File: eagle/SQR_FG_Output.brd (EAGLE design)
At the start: 96.2 x 58.4 mm, 35 parts, among them IC1 MEGA328P, IC2 NJM7032, IC3 7805T, IC4 TLV1117-33, Q1 16MHz, T1 2SK4017, T2 2SK4017

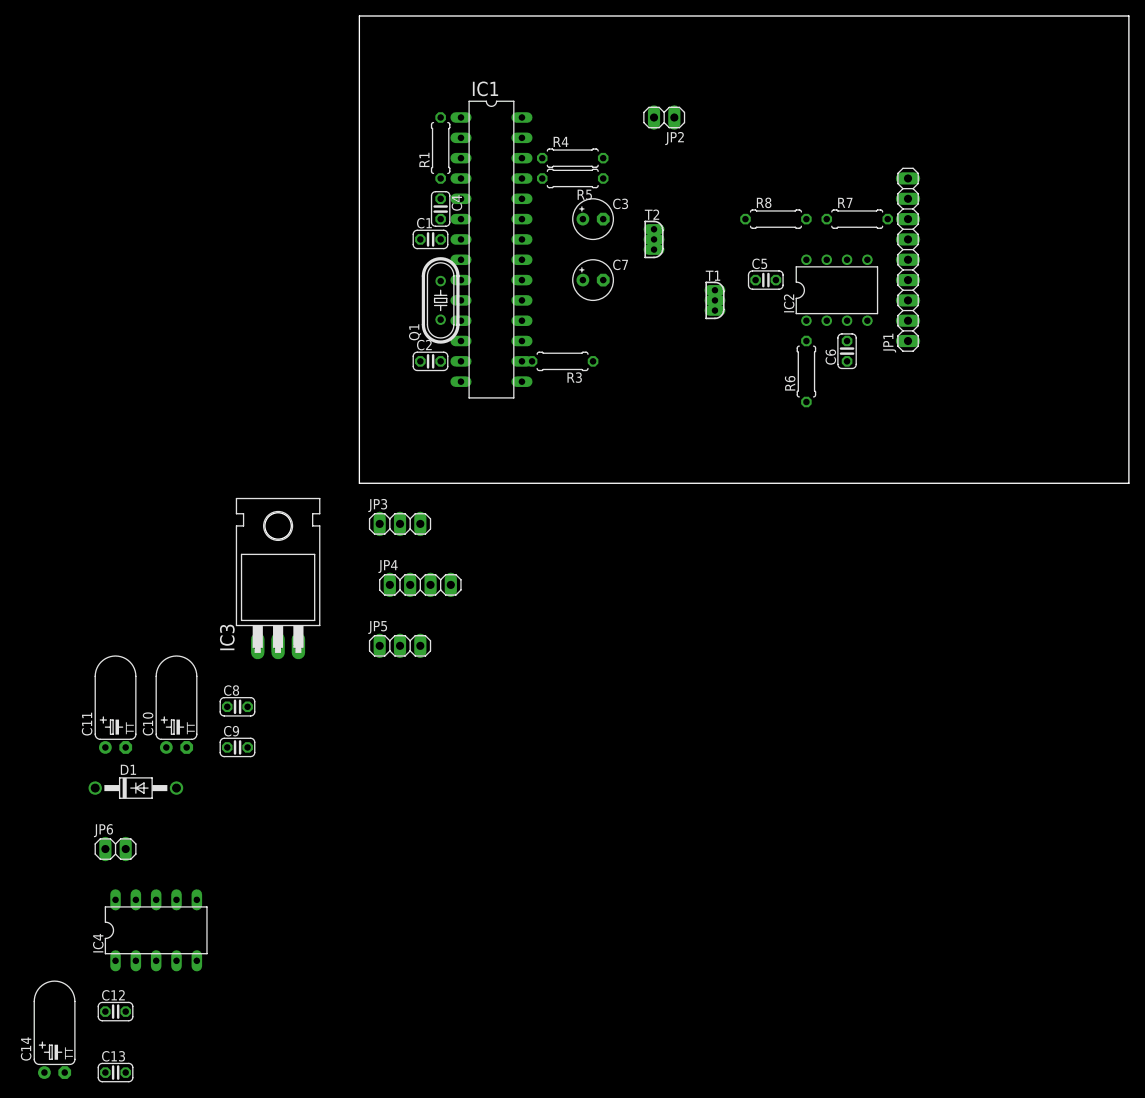
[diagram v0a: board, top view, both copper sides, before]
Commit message: eagle files: デジタル部と出力部に基板を分割
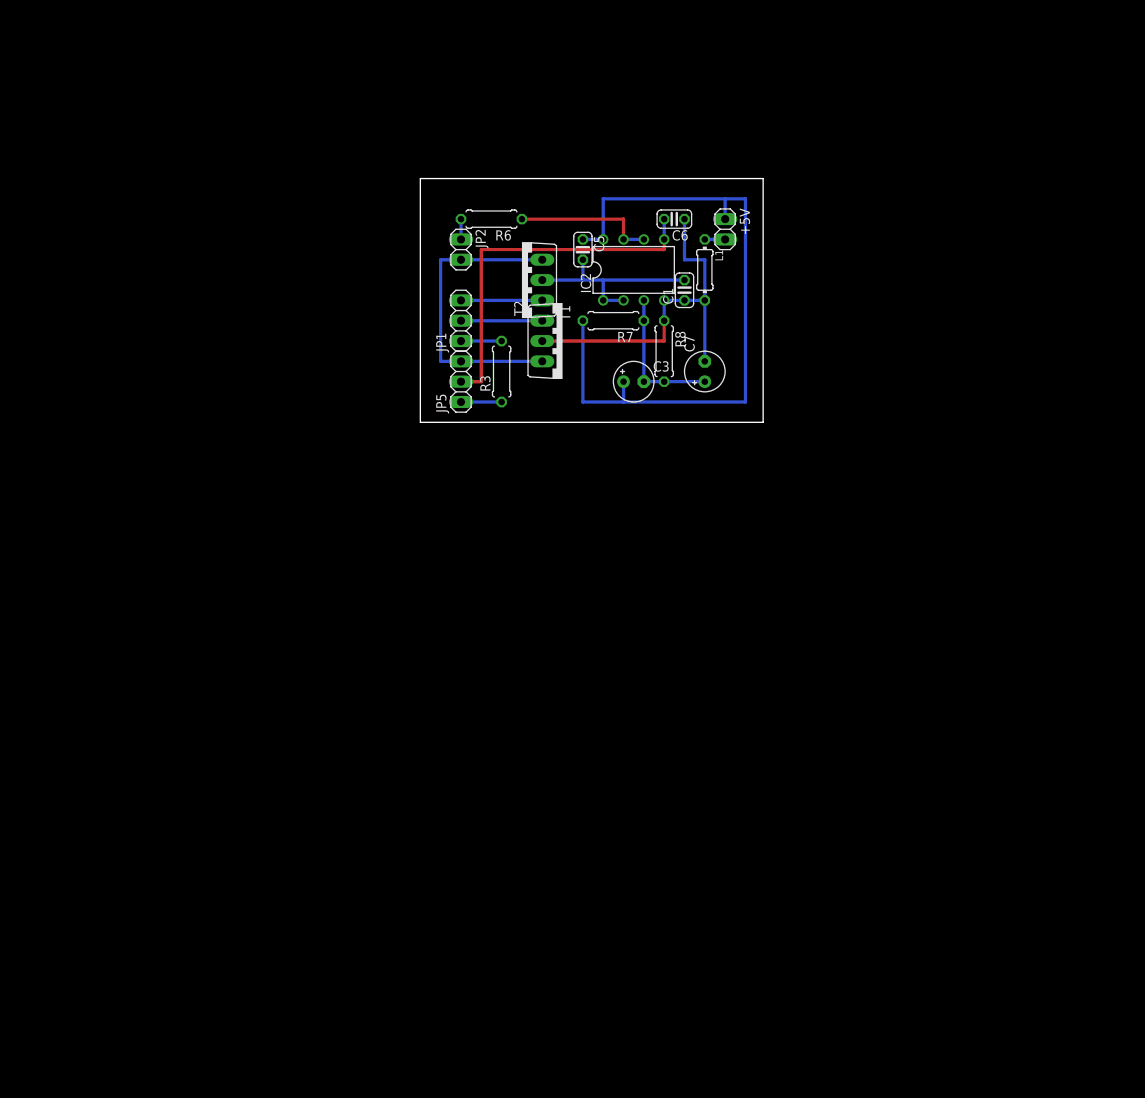
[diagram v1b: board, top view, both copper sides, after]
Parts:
- removed C10, C11, C14: 47uF, rcl:TT2D5L
- removed C12, C13, C4, C8, C9: 0.1uF, rcl:C025-024X044
- removed C2: 22pF, rcl:C025-024X044
- removed D1: 1N4007, diode:DO41-10
- removed IC1: MEGA328P, atmel:DIL28-3
- removed IC3: 7805T, linear:TO220H
- removed IC4: TLV1117-33, ic-package:DIL10
- removed JP3: Duty, pinhead:1X03
- removed JP4: Encoder, pinhead:1X04
- removed JP6: 9V, pinhead:1X02
- removed Q1: 16MHz, crystal:HC49/S
- removed R1: 10k, rcl:0207/7
- removed R4: 22k, rcl:0207/7
- removed R5: 12k, rcl:0207/7
- added +5V: (no value), pinhead:1X02
- added L1: 1uF, rcl:0204/7
- C1: value 22pF -> 0.1uF
- JP1: value I2C-LCD -> DIGITAL_IN; device pinhead:1X09 -> pinhead:1X03
- T1, T2: device zetex:E3LINE -> transistor-power:RD06HVF1
- moved JP1 56.4 mm to (5.08, 12.7)
- moved R6 43.7 mm to (8.89, 25.4), turned to 180 degrees
- moved JP5 33.9 mm to (5.08, 5.08), turned to 90 degrees
- moved R7 33.0 mm to (24.1, 12.7), turned to 180 degrees
- moved C1 32.4 mm to (33.0, 16.5), turned to 90 degrees
- moved JP2 30.3 mm to (5.08, 21.6), turned to 270 degrees
- moved C6 27.2 mm to (31.8, 25.4), turned to 180 degrees
- moved IC2 25.5 mm to (26.7, 19.1)
- moved T1 24.3 mm to (12.7, 17.8), turned to 90 degrees
- moved C5 23.2 mm to (20.3, 21.6), turned to 270 degrees
- moved R8 21.6 mm to (30.5, 8.89), turned to 270 degrees
- moved C3 20.9 mm to (26.7, 5.08)
- moved C7 18.1 mm to (35.6, 6.35), turned to 90 degrees
- moved T2 17.1 mm to (17.8, 10.2), turned to 270 degrees
- moved R3 7.73 mm to (10.2, 6.35), turned to 90 degrees
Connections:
- removed net +3V3: C13.1, IC4.5, JP1.1
- removed net LCD_RST: IC1.26, R4.1
- removed net N$1: C1.2, IC1.9, Q1.2
- removed net N$2: C2.2, IC1.10, Q1.1
- removed net N$3: IC1.1, R1.2
- removed net N$9: IC1.23, JP3.2
- removed net RE_A: IC1.2, JP4.1
- removed net RE_B: IC1.3, JP4.2
- removed net RE_SW: IC1.4, JP4.3
- removed net RST: JP1.7, R4.2, R5.1
- removed net SCL: IC1.28, JP1.6
- removed net SDA: IC1.27, JP1.5
- net +5V: now also +5V.1; no longer C10.+, C11.+, C12.1, C14.+, C4.2, C8.1, C9.1, IC1.20, IC1.7, IC3.1, IC3.3, IC4.3, JP3.1, JP6.1, R1.1
- net AGND: now also C1.1, L1.2, T2.2; no longer C5.2, T2.3
- net GND: now also +5V.2, L1.1; no longer C1.1, C10.-, C11.-, C12.2, C13.2, C14.-, C2.1, C4.1, C8.2, C9.2, IC1.22, IC1.8, IC3.2, IC4.1, JP1.4, JP3.3, JP4.4, JP6.2, R5.2
- net N$15: now also IC2.5; no longer IC2.3
- net N$16: now also IC2.6, IC2.7; no longer IC2.1, IC2.2
- net N$17: now also IC2.3; no longer IC2.5
- net N$6: now also T1.3, T2.3; no longer T1.1, T2.1
- net SW_GND: now also JP1.2, T2.1; no longer IC1.17, T2.2
- net SW_VGND: now also JP1.3, T1.1; no longer IC1.18, T1.2
- net VGND: now also C1.2, C5.2, IC2.1, IC2.2, T1.2; no longer IC2.6, IC2.7, T1.3
- net WAVE_OUT: now also JP1.1; no longer IC1.16
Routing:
- net +5V: track 0.00 -> 86.4 mm
- net AGND: track 0.00 -> 45.7 mm
- net N$15: track 0.00 -> 45.7 mm
- net N$6: track 0.00 -> 38.1 mm
- net VGND: track 0.00 -> 25.4 mm
- net N$17: track 0.00 -> 17.8 mm
- net N$16: track 0.00 -> 17.8 mm
- net SW_VGND: track 0.00 -> 10.2 mm
- net SW_GND: track 0.00 -> 10.2 mm
- net WAVE_OUT: track 0.00 -> 5.08 mm
- net N$8: track 0.00 -> 5.08 mm
- net N$11: track 0.00 -> 2.54 mm
- net GND: track 0.00 -> 2.54 mm
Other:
- board size 96.2 x 58.4 mm -> 42.9 x 30.5 mm

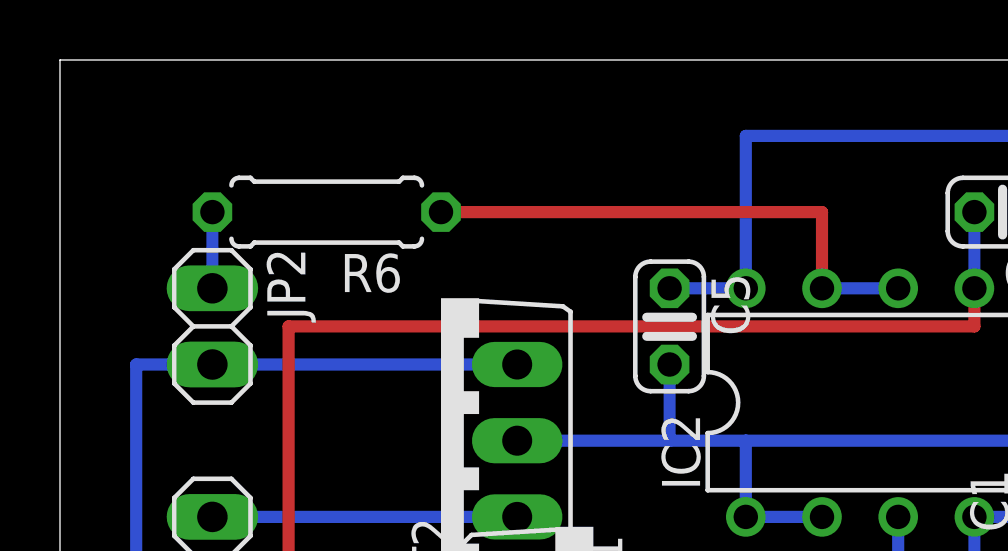
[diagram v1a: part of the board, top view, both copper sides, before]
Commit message: SQR_FG_Digital: I2Cの信号をピンソケットで出力できるように変更
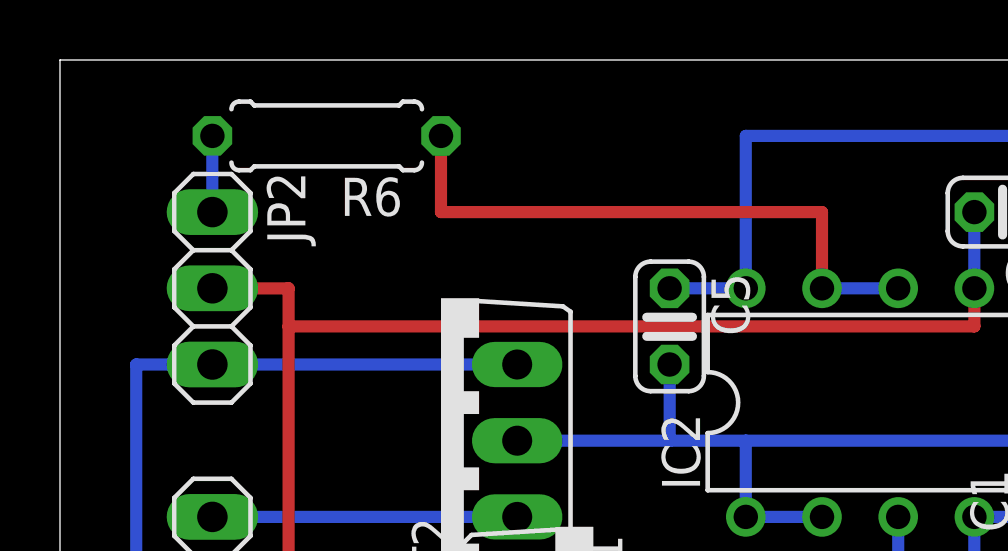
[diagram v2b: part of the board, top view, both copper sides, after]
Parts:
- JP2: value OUT -> (none); device pinhead:1X02 -> pinhead:1X03
- L1: value 1uF -> 1uH
- moved R6 2.54 mm to (8.89, 27.9)
- moved JP2 1.27 mm to (5.08, 22.9)
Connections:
- net N$11 renamed BUFFERD
- removed net N$15: C6.2, IC2.5, JP5.2
- removed net N$6: JP2.2, JP5.3, T1.3, T2.3
- new net BYPASS: C6.2, IC2.5, JP2.2, JP5.2
- new net GND_OUT: JP2.3, JP5.3, T1.3, T2.3
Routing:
- net BYPASS: track 0.00 -> 49.5 mm
- net N$15: track 45.7 -> 0.00 mm
- net GND_OUT: track 0.00 -> 38.1 mm
- net N$6: track 38.1 -> 0.00 mm
- net N$16: track 17.8 -> 20.3 mm
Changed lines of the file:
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@@
 <wire x1="40.64" y1="7.62" x2="2.54" y2="7.62" width="0" layer="101" style="shortdash"/>
 <wire x1="40.64" y1="5.08" x2="2.54" y2="5.08" width="0" layer="101" style="shortdash"/>
+<wire x1="27.94" y1="27.94" x2="27.94" y2="24.13" width="0.4064" layer="100" style="shortdash"/>
+<wire x1="27.94" y1="24.13" x2="35.56" y2="24.13" width="0.4064" layer="100"/>
+<wire x1="35.56" y1="24.13" x2="35.56" y2="27.94" width="0.4064" layer="100" style="shortdash"/>
+<wire x1="35.56" y1="27.94" x2="27.94" y2="27.94" width="0.4064" layer="100"/>
 </plain>
 <attributes>
@@
 <element name="C7" library="rcl" package="E2,5-5" value="100uF" x="35.56" y="6.35" rot="R90"/>
 <element name="IC2" library="linear" package="DIL08" value="NJM7032" x="26.67" y="19.05"/>
-<element name="JP2" library="pinhead" package="1X02" value="OUT" x="5.08" y="21.59" rot="R270"/>
 <element name="JP5" library="pinhead" package="1X03" value="Level" x="5.08" y="5.08" rot="R90"/>
 <element name="R3" library="rcl" package="0207/7" value="10k" x="10.16" y="6.35" rot="R90"/>
-<element name="R6" library="rcl" package="0207/7" value="10" x="8.89" y="25.4" rot="R180"/>
+<element name="R6" library="rcl" package="0207/7" value="10" x="8.89" y="27.94" rot="R180"/>
 <element name="R7" library="rcl" package="0207/7" value="10k" x="24.13" y="12.7" rot="R180"/>
 <element name="R8" library="rcl" package="0207/7" value="10k" x="30.48" y="8.89" rot="R270"/>
@@
 <element name="C1" library="rcl" package="C025-024X044" value="0.1uF" x="33.02" y="16.51" rot="R90"/>
 <element name="+5V" library="pinhead" package="1X02" value="" x="38.1" y="24.13" rot="R270"/>
-<element name="L1" library="rcl" package="0204/7" value="1uF" x="35.56" y="19.05" rot="R270"/>
+<element name="L1" library="rcl" package="0204/7" value="1uH" x="35.56" y="19.05" rot="R270"/>
+<element name="JP2" library="pinhead" package="1X03" value="" x="5.08" y="22.86" rot="R270"/>
 </elements>
 <signals>
@@
 <contactref element="IC2" pad="7"/>
 <wire x1="27.94" y1="22.86" x2="25.4" y2="22.86" width="0.4064" layer="16"/>
-<wire x1="12.7" y1="25.4" x2="25.4" y2="25.4" width="0.4064" layer="1"/>
 <wire x1="25.4" y1="25.4" x2="25.4" y2="22.86" width="0.4064" layer="1"/>
-</signal>
-<signal name="N$11">
+<wire x1="25.4" y1="25.4" x2="12.7" y2="25.4" width="0.4064" layer="1"/>
+<wire x1="12.7" y1="25.4" x2="12.7" y2="27.94" width="0.4064" layer="1"/>
+</signal>
+<signal name="BUFFERD">
 <contactref element="R6" pad="2"/>
 <contactref element="JP2" pad="1"/>
-<wire x1="5.08" y1="22.86" x2="5.08" y2="25.4" width="0.4064" layer="16"/>
+<wire x1="5.08" y1="25.4" x2="5.08" y2="27.94" width="0.4064" layer="16"/>
 </signal>
 <signal name="N$17">
@@
 <wire x1="30.48" y1="5.08" x2="35.56" y2="5.08" width="0.4064" layer="16"/>
 </signal>
-<signal name="N$6">
+<signal name="GND_OUT">
 <contactref element="T1" pad="3"/>
 <contactref element="T2" pad="3"/>
-<contactref element="JP2" pad="2"/>
 <contactref element="JP5" pad="3"/>
 <wire x1="15.24" y1="7.62" x2="5.08" y2="7.62" width="0.4064" layer="16"/>
-<wire x1="5.08" y1="20.32" x2="2.54" y2="20.32" width="0.4064" layer="16"/>
 <wire x1="2.54" y1="20.32" x2="2.54" y2="7.62" width="0.4064" layer="16"/>
 <wire x1="2.54" y1="7.62" x2="5.08" y2="7.62" width="0.4064" layer="16"/>
-<wire x1="5.08" y1="20.32" x2="15.24" y2="20.32" width="0.4064" layer="16"/>
+<contactref element="JP2" pad="3"/>
+<wire x1="15.24" y1="20.32" x2="5.08" y2="20.32" width="0.4064" layer="16"/>
+<wire x1="5.08" y1="20.32" x2="2.54" y2="20.32" width="0.4064" layer="16"/>
 </signal>
 <signal name="SW_GND">
@@
 <wire x1="25.4" y1="15.24" x2="22.86" y2="15.24" width="0.4064" layer="16"/>
 </signal>
-<signal name="N$15">
+<signal name="BYPASS">
 <contactref element="C6" pad="2"/>
 <contactref element="JP5" pad="2"/>
@@
 <wire x1="7.62" y1="21.59" x2="7.62" y2="5.08" width="0.4064" layer="1"/>
 <wire x1="7.62" y1="5.08" x2="5.08" y2="5.08" width="0.4064" layer="1"/>
+<contactref element="JP2" pad="2"/>
+<wire x1="5.08" y1="22.86" x2="7.62" y2="22.86" width="0.4064" layer="1"/>
+<wire x1="7.62" y1="22.86" x2="7.62" y2="21.59" width="0.4064" layer="1"/>
 </signal>
 <signal name="AGND">
